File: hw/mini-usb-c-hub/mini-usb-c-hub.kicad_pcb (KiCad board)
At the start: 4 copper layers, 56 x 30 mm, 38 parts, among them J101 USB_C_Receptacle_USB2.0_16P, J201 USB_A, J301 USB_A, J401 USB_A, P101 USB_C_Plug_USB3.0, U101 FE1.1s, Y101 12MHz

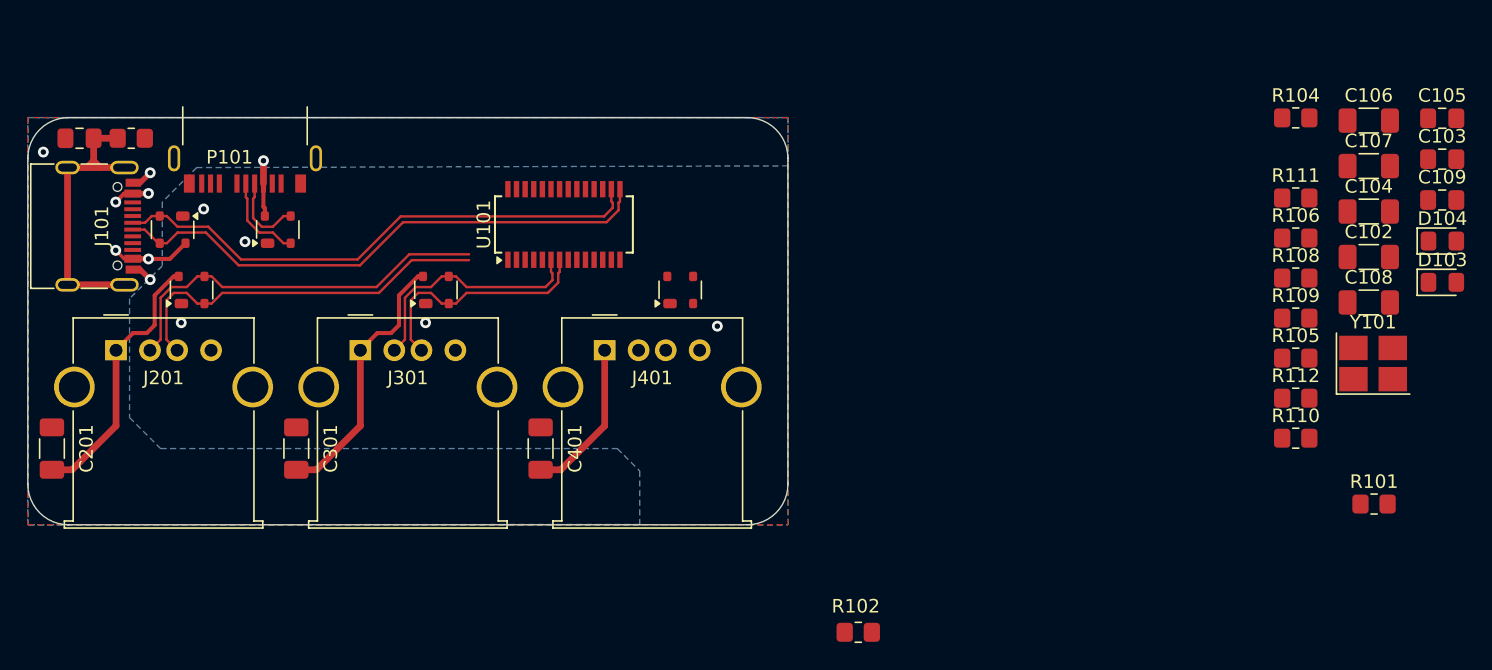
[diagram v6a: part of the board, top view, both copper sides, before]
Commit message: chore(hw): attempt to layout without one USB A
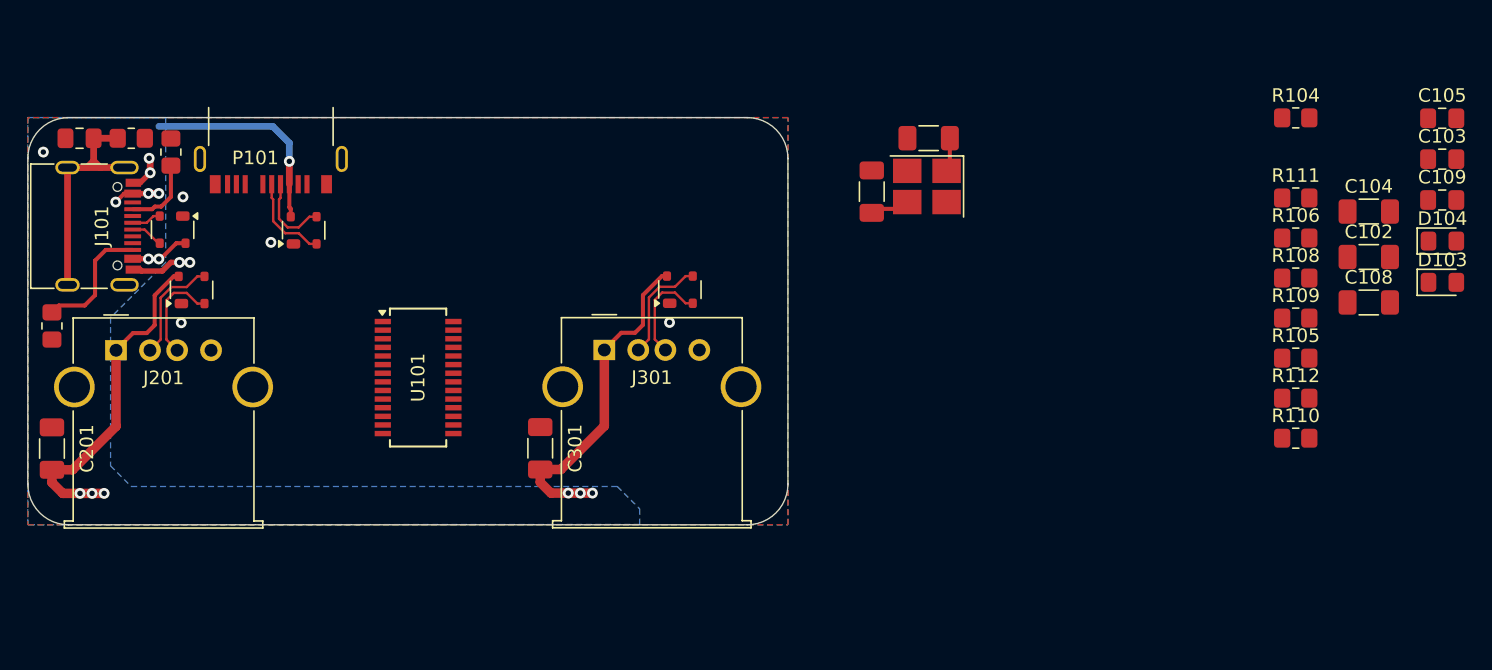
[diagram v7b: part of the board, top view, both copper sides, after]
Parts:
- removed C401: 10u, Capacitor_SMD:C_1206_3216Metric_Pad1.33x1.80mm_HandSolder
- removed D401: PRTR5V0U2X, Package_TO_SOT_SMD:SOT-143
- removed J401: USB_A, Connector_USB:USB_A_Molex_67643_Horizontal
- moved R101 92.4 mm to (124.8, 91.4), turned to 90 degrees
- moved R102 63.5 mm to (116.1, 104.3), turned to -90 degrees
- moved C106 37.0 mm to (176.5, 94.4), turned to -90 degrees
- moved Y101 35.4 mm to (180.5, 94.0), turned to 180 degrees
- moved C107 32.5 mm to (180.7, 90.4)
- moved C301 18.0 mm to (152.1, 113.3)
- moved D301 18.0 mm to (162.3, 101.6)
- moved J301 18.0 mm to (156.8, 106.0)
- moved U101 15.6 mm to (143.1, 108.1), turned to 0 degrees
- moved D102 1.91 mm to (134.6, 97.2)
- moved P101 1.91 mm to (132.2, 91.9)
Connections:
- D201 pad 2: /D4USB+ -> /D3USB+
- D201 pad 3: /D4USB- -> /D3USB-
- D301 pad 2: /D3USB+ -> /D2USB+
- D301 pad 3: /D3USB- -> /D2USB-
- J201 pad 2: /D4USB- -> /D3USB-
- J201 pad 3: /D4USB+ -> /D3USB+
- J301 pad 2: /D3USB- -> /D2USB-
- J301 pad 3: /D3USB+ -> /D2USB+
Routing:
- net /UUSB-: track 40.8 -> 2.41 mm
- net /UUSB+: track 39.9 -> 2.20 mm
- net /D4USB-: track 28.9 -> 0.00 mm
- net /D4USB+: track 28.2 -> 0.00 mm
- net /D3USB+: track 17.8 -> 7.36 mm
- net /D3USB-: track 17.8 -> 8.07 mm
- net +5V: track 63.9 -> 73.3 mm, vias 5 -> 12
- net Net-(J101-CC2): track 0.00 -> 9.34 mm
- net /D2USB-: track 0.00 -> 8.07 mm
- net /D2USB+: track 0.00 -> 7.36 mm
- net Net-(J101-CC1): track 0.00 -> 5.49 mm
- net Net-(J101-SHIELD): track 23.3 -> 19.1 mm
- net GND: track 3.11 -> 7.13 mm, vias 8 -> 9
- net Net-(U101-XOUT): track 0.00 -> 2.94 mm
- net Net-(U101-XIN): track 0.00 -> 2.51 mm

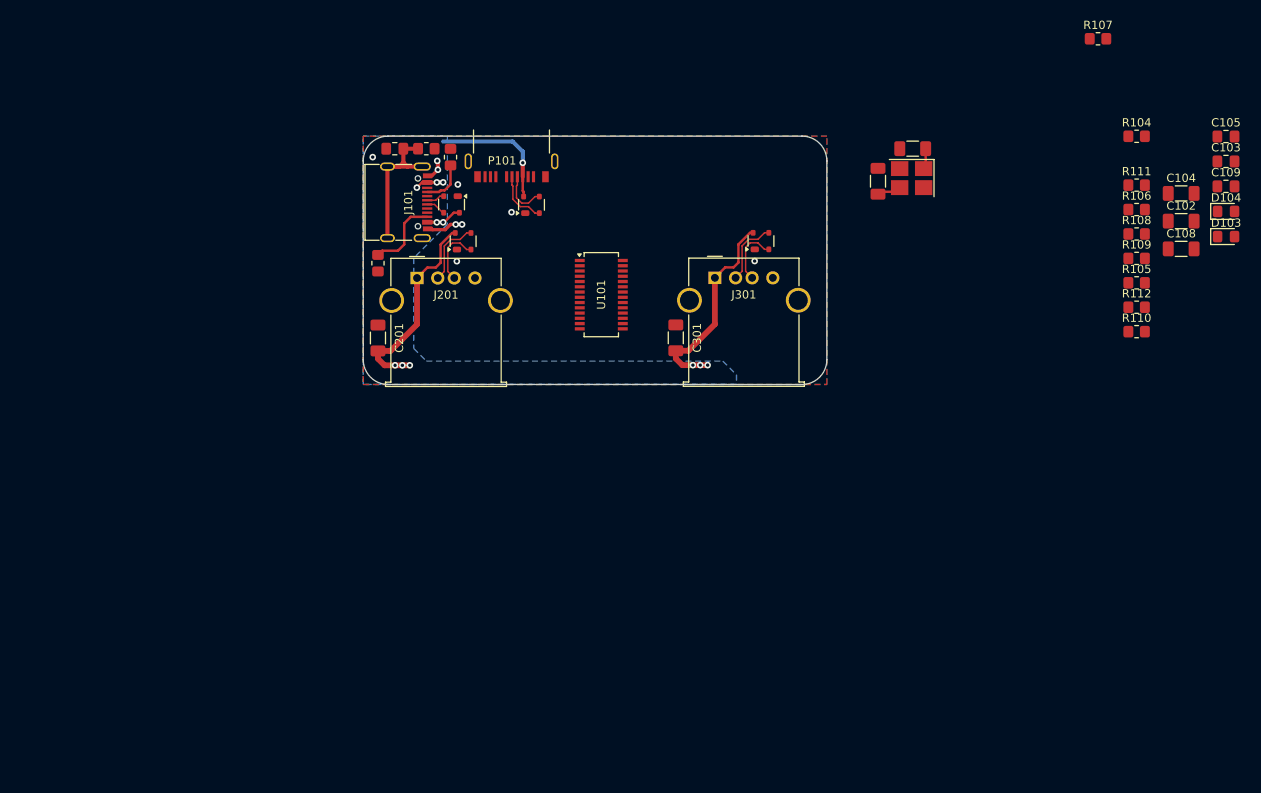
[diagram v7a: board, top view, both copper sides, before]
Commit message: chore(hw): layout support components
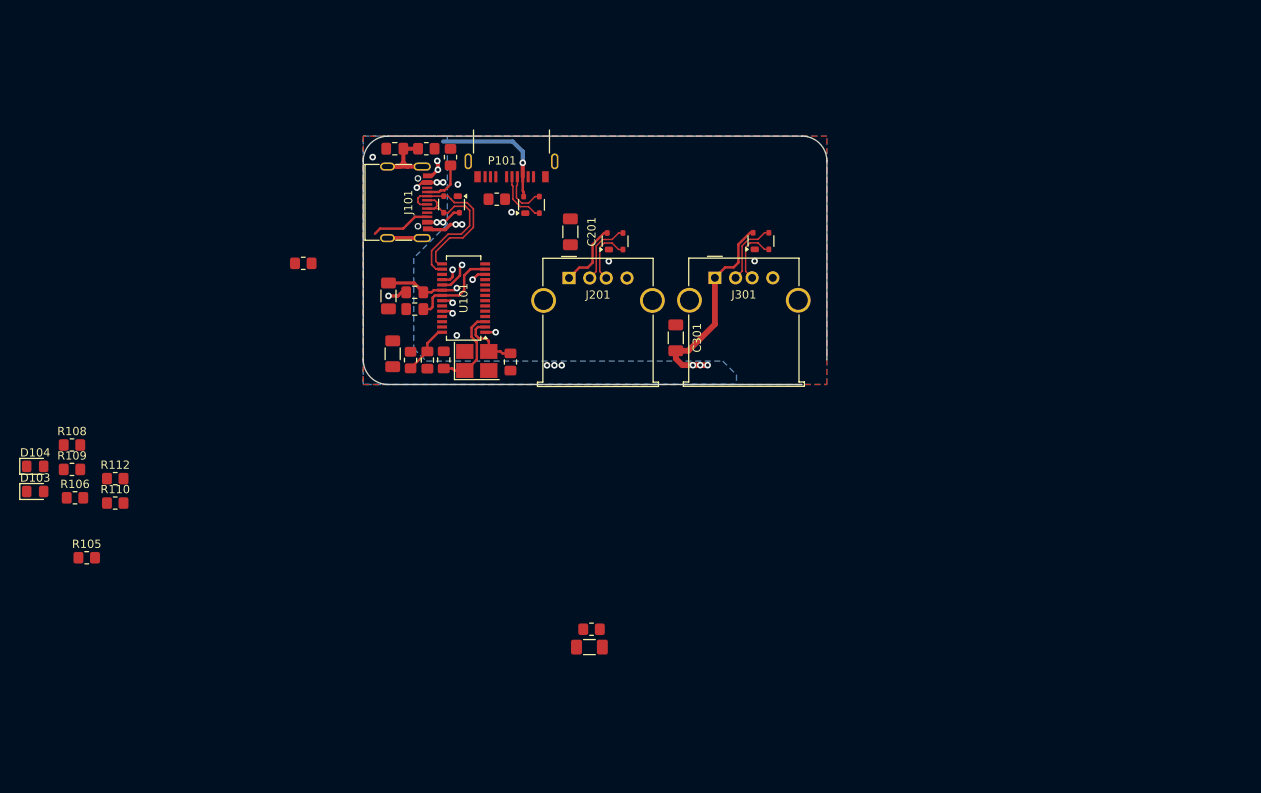
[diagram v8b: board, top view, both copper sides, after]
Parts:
- C106, C107: footprint Capacitor_SMD:C_1206_3216Metric_Pad1.33x1.80mm_HandSolder -> Capacitor_SMD:C_0805_2012Metric_Pad1.18x1.45mm_HandSolder
- moved D103 147.1 mm to (74.7, 131.8)
- moved D104 147.1 mm to (74.7, 128.8)
- moved R106 132.9 mm to (79.5, 132.6)
- moved R108 131.1 mm to (79.1, 126.2)
- moved R109 131.1 mm to (79.1, 129.2)
- moved R105 131.1 mm to (80.9, 139.8)
- moved R110 125.1 mm to (84.3, 133.2)
- moved R112 125.1 mm to (84.3, 130.3)
- moved C105 100.2 mm to (122.0, 116.0), turned to -90 degrees
- moved C103 99.6 mm to (120.5, 109.8), turned to 180 degrees
- moved C109 98.8 mm to (120.5, 107.8)
- moved C102 96.6 mm to (117.9, 115.2), turned to -90 degrees
- moved C108 95.9 mm to (117.3, 108.2), turned to 90 degrees
- moved R104 91.8 mm to (120.0, 116.0), turned to -90 degrees
- moved C104 90.1 mm to (141.6, 150.6), turned to 180 degrees
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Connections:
- D101 pad 2: /UUSB+ -> /UUSB-
- D101 pad 3: /UUSB- -> /UUSB+
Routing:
- net /UUSB+: track 2.20 -> 19.8 mm
- net /UUSB-: track 2.41 -> 19.2 mm
- net +3.3V: track 0.00 -> 11.2 mm
- net Net-(U101-XIN): track 2.51 -> 10.7 mm
- net +5V: track 73.3 -> 65.4 mm, vias 12 -> 13
- net Net-(U101-VD18): track 0.00 -> 6.20 mm
- net Net-(U101-XOUT): track 2.94 -> 7.81 mm
- net Net-(J101-SHIELD): track 19.1 -> 23.3 mm
- net Net-(U101-BUSJ): track 0.00 -> 4.01 mm, vias 0 -> 1
- net GND: track 7.13 -> 10.7 mm, vias 9 -> 12
- net Net-(U101-VBUSM): track 0.00 -> 2.28 mm, vias 0 -> 1
- net Net-(J101-CC2): track 9.34 -> 7.16 mm
- net Net-(U101-VD18_O): track 0.00 -> 1.78 mm, vias 0 -> 1
- net Net-(U101-DRV): track 0.00 -> 1.38 mm, vias 0 -> 1
- net Net-(D103-K): track 0.00 -> 1.38 mm, vias 0 -> 1
